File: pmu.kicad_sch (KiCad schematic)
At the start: 18 parts, among them J4 Battery, SW1 POWER ON/OFF, U3 MAX1555, U4 MAX16054, U5 TPS63031DSK

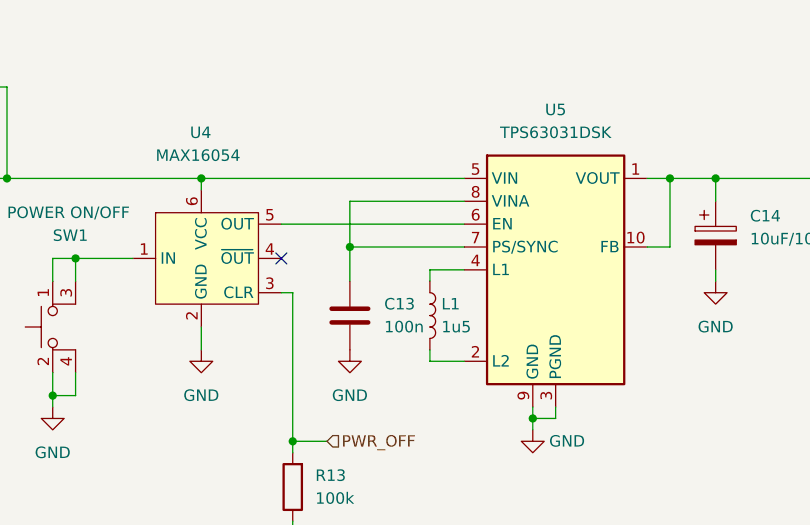
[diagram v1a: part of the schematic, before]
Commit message: `PS/SYNC` tied to GND
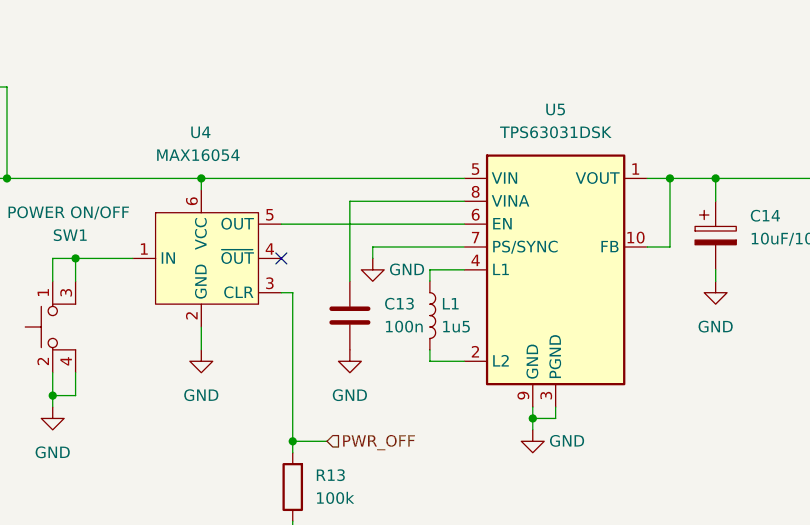
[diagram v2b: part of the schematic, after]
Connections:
- net GND: now also U5.7 (PS/SYNC)
- net at C13.2, U5.8 (VINA): no longer U5.7 (PS/SYNC)
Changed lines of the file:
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@@
 	(title_block
 		(title "Mainboard replacement for Nokia 3310")
-		(date "24-01-2025")
+		(date "29-01-2025")
 		(rev "Rev A")
 		(company "M17 Project")
@@
 	)
 	(junction
-		(at 147.32 91.44)
-		(diameter 0)
-		(color 0 0 0 0)
-	)
-	(junction
 		(at 74.93 104.14)
 		(diameter 0)
@@
 	(wire
 		(pts
+			(xy 160.02 91.44) (xy 149.86 91.44)
+		)
+		(stroke
+			(width 0)
+			(type default)
+		)
+	)
+	(wire
+		(pts
 			(xy 95.25 91.44) (xy 95.25 104.14)
 		)
@@
 	(wire
 		(pts
-			(xy 147.32 91.44) (xy 147.32 95.25)
+			(xy 147.32 86.36) (xy 147.32 95.25)
 		)
 		(stroke
@@
 	(wire
 		(pts
-			(xy 147.32 86.36) (xy 147.32 91.44)
-		)
-		(stroke
-			(width 0)
-			(type default)
-		)
-	)
-	(wire
-		(pts
 			(xy 83.82 91.44) (xy 86.36 91.44)
 		)
@@
 	(wire
 		(pts
-			(xy 147.32 91.44) (xy 160.02 91.44)
+			(xy 149.86 91.44) (xy 149.86 92.71)
 		)
 		(stroke
@@
 					(unit 1)
 				)
+			)
+		)
+	)
+	(symbol
+		(lib_id "power:GND")
+		(at 149.86 92.71 0)
+		(unit 1)
+		(exclude_from_sim no)
+		(in_bom yes)
+		(on_board yes)
+		(dnp no)
+		(property "Reference" "#PWR070"
+			(at 149.86 99.06 0)
+			(effects
+				(font
+					(size 1.27 1.27)
+				)
+				(hide yes)
+			)
+		)
+		(property "Value" "GND"
+			(at 153.67 93.98 0)
+			(effects
+				(font
+					(size 1.27 1.27)
+				)
+			)
+		)
+		(property "Footprint" ""
+			(at 149.86 92.71 0)
+			(effects
+				(font
+					(size 1.27 1.27)
+				)
+				(hide yes)
+			)
+		)
+		(property "Datasheet" ""
+			(at 149.86 92.71 0)
+			(effects
+				(font
+					(size 1.27 1.27)
+				)
+				(hide yes)
+			)
+		)
+		(property "Description" "Power symbol creates a global label with name \"GND\" , ground"
+			(at 149.86 92.71 0)
+			(effects
+				(font
+					(size 1.27 1.27)
+				)
+				(hide yes)
+			)
+		)
+		(pin "1"
+		)
+		(instances
+			(project "M17_3310"
+				(path "/8d65c5ef-7a02-4454-aee5-ab9c49e4aeab/69b4d1b1-805b-4c7a-b583-ffe559937ec6"
+					(reference "#PWR070")
+					(unit 1)
+				)
